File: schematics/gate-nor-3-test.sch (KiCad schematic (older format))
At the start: 4 parts

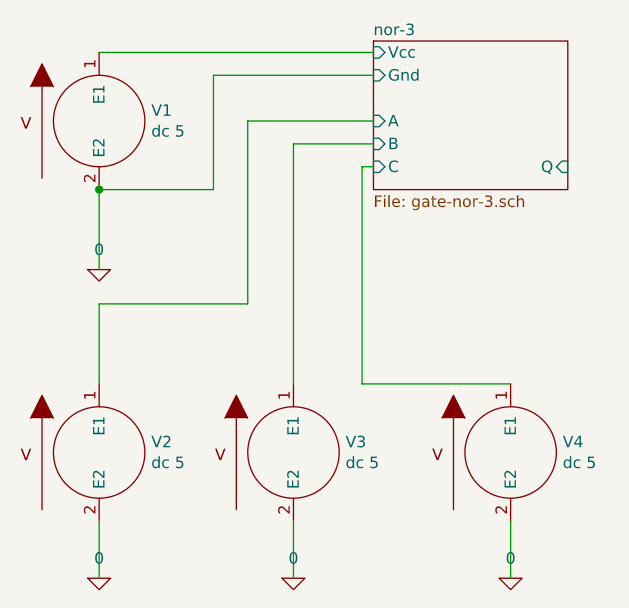
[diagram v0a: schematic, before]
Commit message: Adds some tests for and-2, nor-2, nor-3
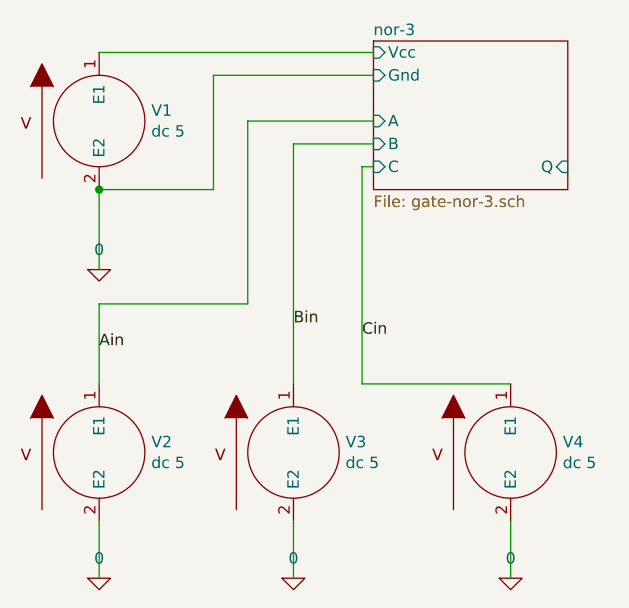
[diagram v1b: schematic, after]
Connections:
- net nor-3/A renamed Ain
- net nor-3/B renamed Bin
- net nor-3/C renamed Cin
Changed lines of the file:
@@
 EESchema Schematic File Version 4
+LIBS:gate-nor-3-test-cache
 EELAYER 26 0
 EELAYER END
@@
 $EndComp
 $Comp
-L pspice:0 #GND0101
+L pspice:0 #GND01
 U 1 1 5C401538
 P 3700 3950
-F 0 "#GND0101" H 3700 3850 50  0001 C CNN
+F 0 "#GND01" H 3700 3850 50  0001 C CNN
 F 1 "0" H 3700 4037 50  0000 C CNN
 F 2 "" H 3700 3950 50  0001 C CNN
@@
 $EndComp
 $Comp
-L pspice:0 #GND0102
+L pspice:0 #GND02
 U 1 1 5C401A79
 P 3700 5300
-F 0 "#GND0102" H 3700 5200 50  0001 C CNN
+F 0 "#GND02" H 3700 5200 50  0001 C CNN
 F 1 "0" H 3700 5387 50  0000 C CNN
 F 2 "" H 3700 5300 50  0001 C CNN
@@
 $EndComp
 $Comp
-L pspice:0 #GND0103
+L pspice:0 #GND03
 U 1 1 5C401D5F
 P 4550 5300
-F 0 "#GND0103" H 4550 5200 50  0001 C CNN
+F 0 "#GND03" H 4550 5200 50  0001 C CNN
 F 1 "0" H 4550 5387 50  0000 C CNN
 F 2 "" H 4550 5300 50  0001 C CNN
@@
 $EndComp
 $Comp
-L pspice:0 #GND0104
+L pspice:0 #GND04
 U 1 1 5C401DF2
 P 5500 5300
-F 0 "#GND0104" H 5500 5200 50  0001 C CNN
+F 0 "#GND04" H 5500 5200 50  0001 C CNN
 F 1 "0" H 5500 5387 50  0000 C CNN
 F 2 "" H 5500 5300 50  0001 C CNN
@@
 Wire Wire Line
 	4850 4450 5500 4450
+Text Label 3700 4300 0    50   ~ 0
+Ain
+Text Label 4550 4200 0    50   ~ 0
+Bin
+Text Label 4850 4250 0    50   ~ 0
+Cin
 $EndSCHEMATC
